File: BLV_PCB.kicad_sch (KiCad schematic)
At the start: 15 parts, among them J1 JST-PH, J2 JST-PH, J3 JST-PH, J4 PinHeader_01x03_Pin, J5 PinHeader_01x03_Pin, J6 PinHeader_01x03_Pin

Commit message: Add 10k pull-ups to SDcard
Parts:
- removed R1, R2: 10k, Resistor_SMD:R_0402_1005Metric, symbol Device:R
- J7: renamed from J?; footprint (none) -> Connector_PinHeader_2.54mm:PinHeader_2x03_P2.54mm_Vertical

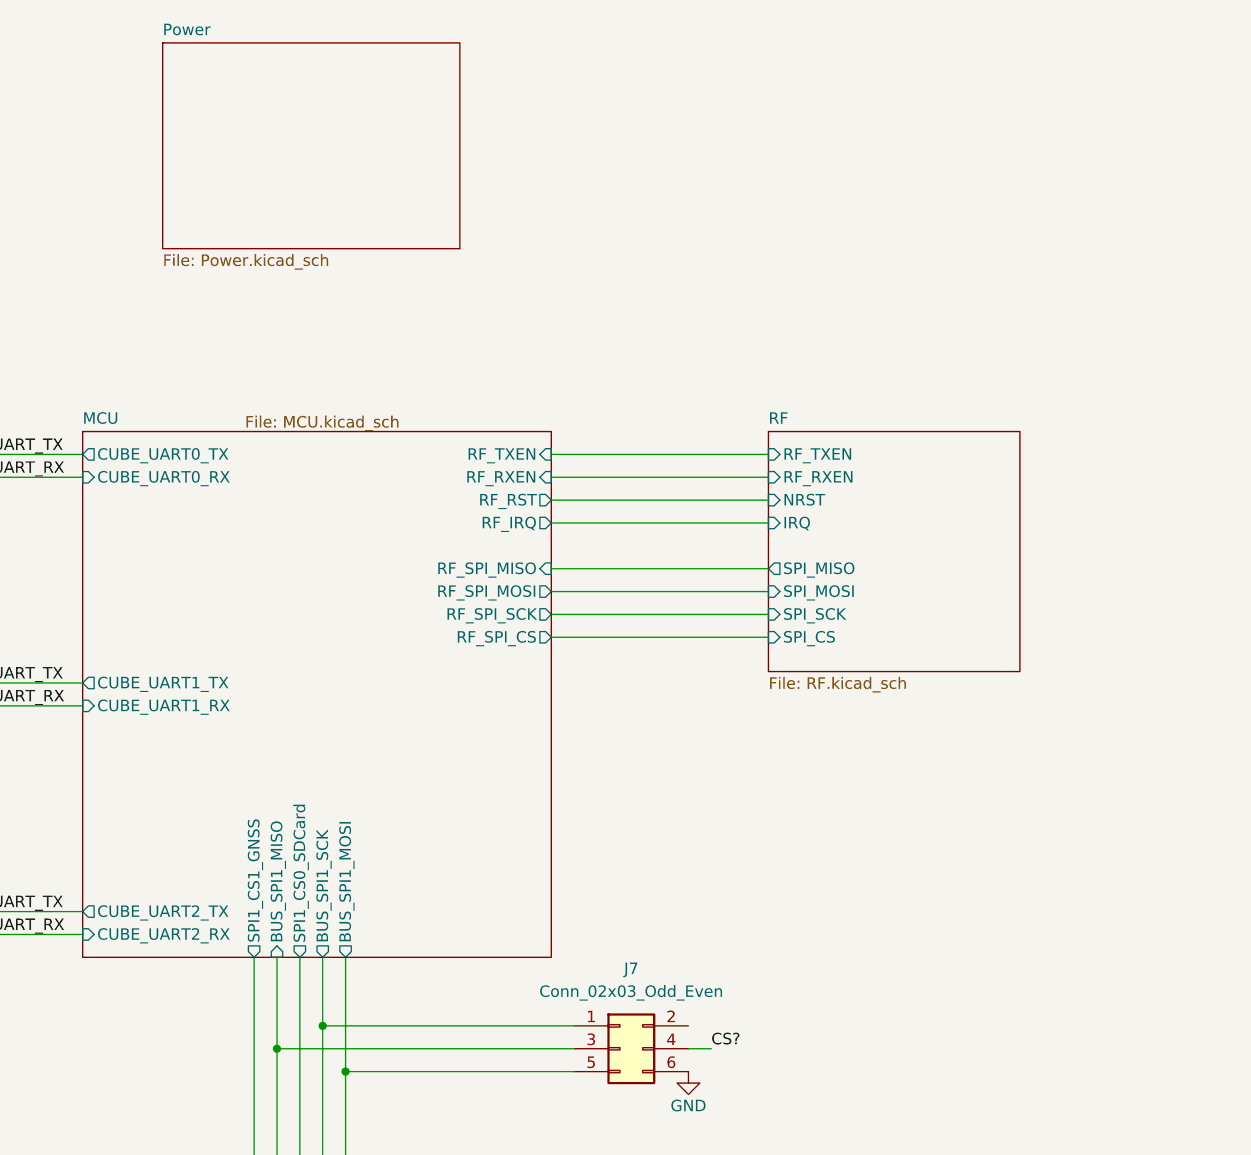
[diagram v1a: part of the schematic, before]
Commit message: discrete protection, charger, ideal diodes, and 5v smps
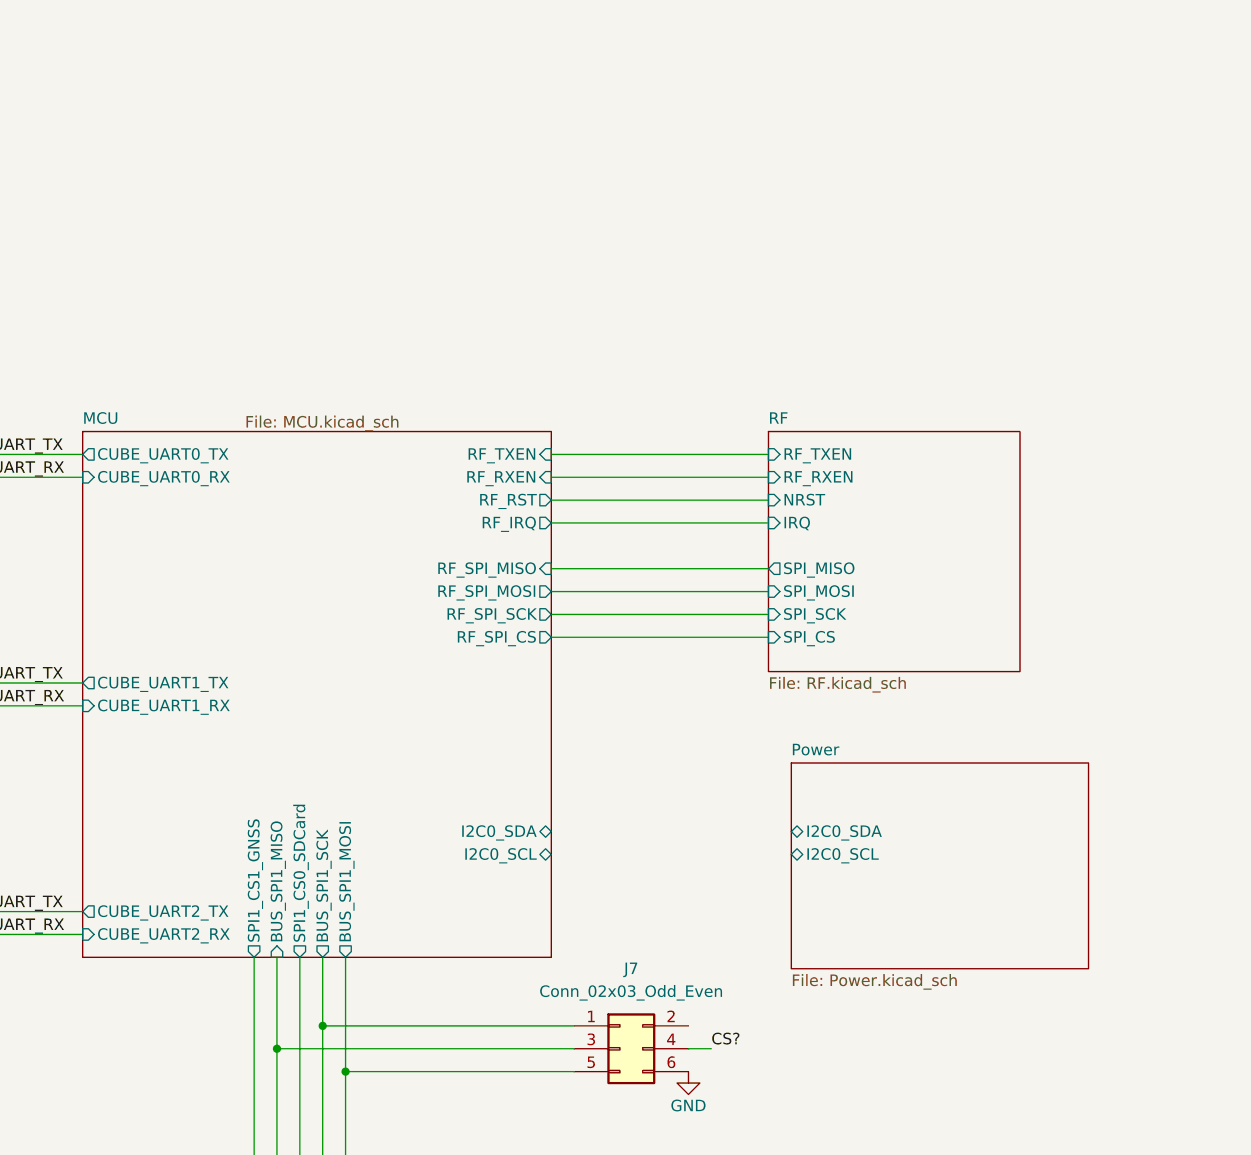
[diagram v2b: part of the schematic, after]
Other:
- sheet MCU ports: added I2C0_SCL, I2C0_SDA; removed none
- sheet Power ports: added I2C0_SCL, I2C0_SDA; removed none
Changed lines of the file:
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@@
 	)
 	(sheet
-		(at 148.59 33.02)
+		(at 218.44 113.03)
 		(size 33.02 22.86)
 		(exclude_from_sim no)
@@
 		)
 		(property "Sheetname" "Power"
-			(at 148.59 32.3084 0)
+			(at 218.44 112.3184 0)
 			(effects
 				(font
@@
 		)
 		(property "Sheetfile" "Power.kicad_sch"
-			(at 148.59 56.4646 0)
+			(at 218.44 136.4746 0)
 			(effects
 				(font
@@
 		)
 		(property "Field2" ""
-			(at 148.59 33.02 0)
-			(effects
-				(font
-					(size 1.27 1.27)
-				)
+			(at 218.44 113.03 0)
+			(effects
+				(font
+					(size 1.27 1.27)
+				)
+			)
+		)
+		(pin "I2C0_SCL" bidirectional
+			(at 218.44 123.19 180)
+			(effects
+				(font
+					(size 1.27 1.27)
+				)
+				(justify left)
+			)
+		)
+		(pin "I2C0_SDA" bidirectional
+			(at 218.44 120.65 180)
+			(effects
+				(font
+					(size 1.27 1.27)
+				)
+				(justify left)
 			)
 		)
@@
 			(effects
 				(font
+					(size 1.27 1.27)
+				)
+				(justify right)
+			)
+		)
+		(pin "I2C0_SCL" bidirectional
+			(at 191.77 123.19 0)
+			(effects
+				(font
+					(size 1.27 1.27)
+				)
+				(justify right)
+			)
+		)
+		(pin "I2C0_SDA" bidirectional
+			(at 191.77 120.65 0)
+			(effects
+				(font
